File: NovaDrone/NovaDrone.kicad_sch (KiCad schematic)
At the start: 0 parts

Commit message: End of Inverter design
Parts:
- added C10, C11, C12, C13, C9: 15nF, Capacitor_SMD:C_0603_1608Metric, symbol Device:C
- added C3, C5, C7: 0.1uF, Capacitor_SMD:C_0603_1608Metric, symbol Device:C
- added D9: SS0540_R1_00001, BassingaLib_Diodes:SOD3816X135N, symbol BassingaLib_Diodes:SS0540_R1_00001
- added IC1, IC2, IC3: UCC27211DR, BassingaLib_BridgeDRVR:SOIC127P600X175-8N, symbol BassingaLib_BridgeDRVR:UCC27211DR
- added R17, R27, R29, R36, R37: 33k 1%, Resistor_SMD:R_0603_1608Metric, symbol Device:R
- added R26, R28, R30: 4.7k 1%, Resistor_SMD:R_0603_1608Metric, symbol Device:R
- added R31: 180k 1%, Resistor_SMD:R_0603_1608Metric, symbol Device:R
- added R32, R33, R34: 680R 1%, Resistor_SMD:R_0603_1608Metric, symbol Device:R
- added R35: 18k 1%, Resistor_SMD:R_0603_1608Metric, symbol Device:R
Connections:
- new net: C5.1, IC2.2 (HB)
- new net: C7.1, IC3.2 (HB)
- new net: C3.1, IC1.2 (HB)
- new net +10V: IC1.1 (VDD), IC2.1 (VDD), IC3.1 (VDD)
- new net +3.3V: D9.1 (K), R36.2
- new net GND: C12.1, C13.1, IC1.7 (VSS), IC2.7 (VSS), IC3.7 (VSS), R26.1, R28.1, R30.1, R35.1, R37.1
- new net Half-Bridge_1/G_H: IC1.3 (HO)
- new net Half-Bridge_1/G_L: IC1.8 (LO)
- new net Half-Bridge_1/HS: C3.2, IC1.4 (HS)
- new net Half-Bridge_1/Vshunt_B: R34.1
- new net Half-Bridge_2/G_H: IC2.3 (HO)
- new net Half-Bridge_2/G_L: IC2.8 (LO)
- new net Half-Bridge_2/HS: C5.2, IC2.4 (HS)
- new net Half-Bridge_2/Vshunt_B: R33.1
- new net Half-Bridge_3/G_H: IC3.3 (HO)
- new net Half-Bridge_3/G_L: IC3.8 (LO)
- new net Half-Bridge_3/HS: C7.2, IC3.4 (HS)
- new net Half-Bridge_3/Vshunt_B: R32.1
- new net OUT1: R17.1, R27.1, R29.1
- new net Phase_1: R17.2, R26.2, R27.2, R28.2, R29.2, R30.2
- new net Power_GND: C10.1, C11.1, C9.1
- new net V3.3_Mesure: C13.2, R36.1, R37.2
- new net Vbus_Mesure: C12.2, D9.2 (A), R31.1, R35.2
- new net Vshunt_1: C11.2, R34.2
- new net Vshunt_2: C10.2, R33.2
- new net Vshunt_3: C9.2, R32.2
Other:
- added sheet Half-Bridge_1 (Half_Bridge.kicad_sch)
- added sheet Half-Bridge_2 (Half_Bridge.kicad_sch)
- added sheet Half-Bridge_3 (Half_Bridge.kicad_sch)
- note added: "+3.3V Mesurement"
- note added: "Back-EMF Sensing"
- note added: "Half-Bridge Driver"
- note added: "PCB Temperature Mesurement"
- note added: "Power Invertor"
- note added: "Voltage Bus Mesurement"

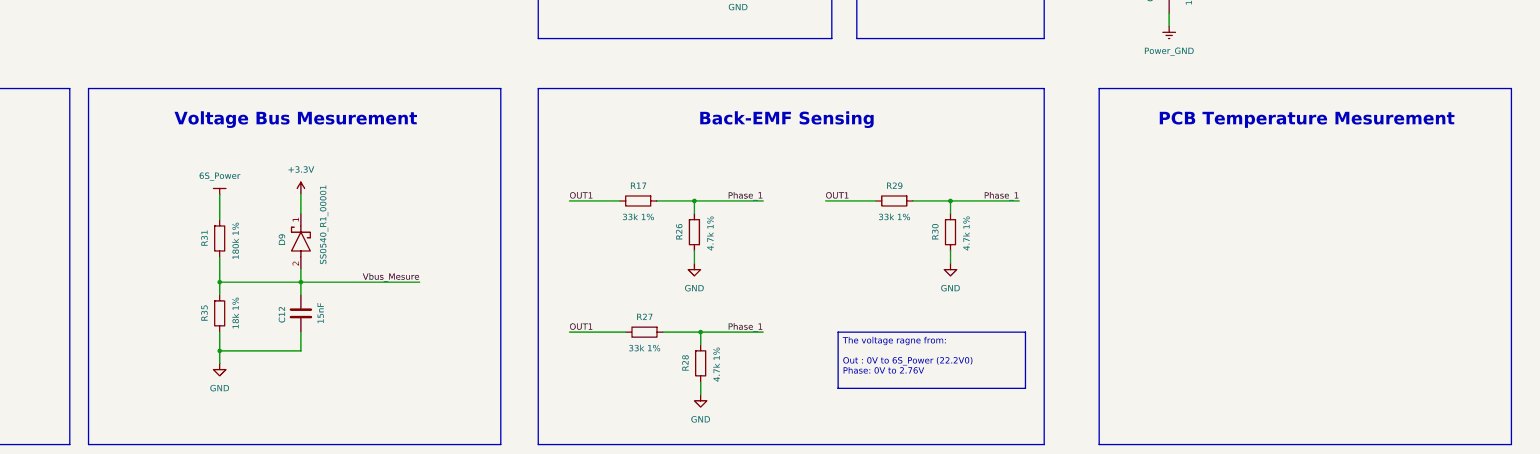
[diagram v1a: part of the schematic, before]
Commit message: PCB temperature measurement
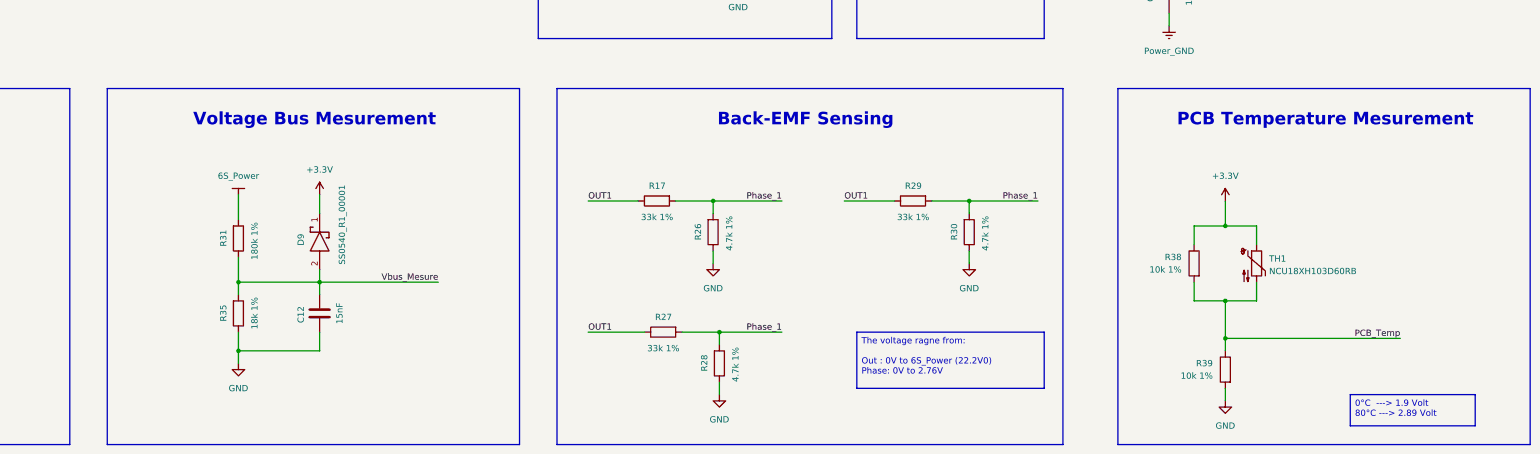
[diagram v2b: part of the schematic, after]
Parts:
- added R38, R39: 10k 1%, Resistor_SMD:R_0603_1608Metric, symbol Device:R
- added TH1: NCU18XH103D60RB, Resistor_SMD:R_0603_1608Metric, symbol Device:Thermistor_NTC
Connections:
- net +3.3V: now also R38.1, TH1.1
- net GND: now also R39.2
- new net PCB_Temp: R38.2, R39.1, TH1.2
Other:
- moved on the sheet: C12, D9, R17, R26, R27, R28, R29, R30, R31, R35

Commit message: Update 10.07.2025
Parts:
- added C14: 15nF, Capacitor_SMD:C_0603_1608Metric, symbol Device:C
- added D10: SS0540_R1_00001, BassingaLib_Diodes:SOD3816X135N, symbol BassingaLib_Diodes:SS0540_R1_00001
- added R40: 68k 1%, Resistor_SMD:R_0603_1608Metric, symbol Device:R
- added R42: 10k 1%, Resistor_SMD:R_0603_1608Metric, symbol Device:R
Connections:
- net +10V: now also R40.2
- net +3.3V: now also D10.1 (K)
- net GND: now also C14.1, R42.2
- net Phase_1: no longer R27.2, R28.2, R29.2, R30.2
- net MCU/PWM_C_H: now reaches IC3.5 (HI)
- net MCU/PWM_C_L: now reaches IC3.6 (LI)
- net MCU/PWM_A_H: now reaches IC1.5 (HI)
- net MCU/PWM_A_L: now reaches IC1.6 (LI)
- net MCU/PWM_B_H: now reaches IC2.5 (HI)
- net MCU/PWM_B_L: now reaches IC2.6 (LI)
- new net Phase_2: R29.2, R30.2
- new net Phase_3: R27.2, R28.2
- new net V10_Mesure: C14.2, D10.2 (A), R40.1, R42.1
- no-connect marks 0 -> 1
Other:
- added sheet MCU (MCU.kicad_sch)
- note added: "+10V Mesurement"
- moved on the sheet: C10, C11, C12, C13, C3, C5, C7, C9, D9, IC1, IC2, IC3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

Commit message: Interfaces Update
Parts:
- added C18, C19, C20, C34, C35: 1uF 50V, Capacitor_SMD:C_0805_2012Metric, symbol Device:C
- added C28, C29, C30: 0.1uF 50V, Capacitor_SMD:C_0603_1608Metric, symbol Device:C
- added D11: PESD2CANFD24V-TR, BassingaLib_TVS:SOT95P230X110-3N, symbol BassingaLib_TVS:PESD2CANFD24V-TR
- added D3: PESD3V3S2UT,215, BassingaLib_TVS:SOT95P230X110-3N, symbol BassingaLib_TVS:PESD3V3S2UT,215
- added IC5: TCAN3403DDFRQ1, BassinaLib_Com_Interfaces:SOT65P280X110-8N, symbol BassinaLib_Com_Interfaces:TCAN3403DDFRQ1
- added J1: JST SH 3Pin, BassinaLib_Connectors:JST_BM03B-SRSS-TB_LF__SN_, symbol BassinaLib_Connectors:BM03B-SRSS-TB_LF__SN_
- added J2: JST SH 5Pin, BassinaLib_Connectors:JST_BM05B-SRSS-TB_LF__SN_, symbol BassinaLib_Connectors:BM05B-SRSS-TB_LF__SN_
- added J3: JST SH 4Pin, BassinaLib_Connectors:ADAFRUIT_4328, symbol BassinaLib_Connectors:4328
- added R45, R46: 22R 1%, Resistor_SMD:R_0603_1608Metric, symbol Device:R
- added R47: 120R 1%, Resistor_SMD:R_0603_1608Metric, symbol Device:R
- added S1: DS04-254-2-01BK-SMT, BassinaLib_Switch:DS04254201BKSMT, symbol BassinaLib_Switch:DS04-254-2-01BK-SMT
- C3, C5, C7: value 0.1uF -> 0.1uF 50V
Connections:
- net +10V: now also C18.2, C19.2, C20.2
- net +3.3V: now also C34.1, C35.1, IC5.3 (V_CC), IC5.5 (VIO), J2.1, J3.1
- net GND: now also C18.1, C19.1, C20.1, C28.1, C29.1, C30.1, C34.2, C35.2, D11.3, D3.3, IC5.2 (GND), J1.2, J1.S1 (SHIELD), J1.S2 (SHIELD), J2.5, J2.S1 (SHIELD), J2.S2 (SHIELD), J3.4, J3.SH1 (SHIELD), J3.SH2 (SHIELD)
- net MCU/FDCAN2_RX: now also IC5.4 (RXD)
- net MCU/FDCAN2_TX: now also IC5.1 (TXD)
- net MCU/SWCLK: now also J2.3
- net MCU/SWDIO: now also J2.2
- net MCU/UART2_RX: now also D3.1, R46.2
- net MCU/UART2_TX: now also D3.2, R45.2
- net MCU/nRST: now also J2.4
- net Phase_1: now also C28.2
- net Phase_2: now also C30.2
- net Phase_3: now also C29.2
- new net: J1.1, R46.1
- new net: J1.3, R45.1
- new net: R47.2, S1.1
- new net CANH: D11.1, IC5.7 (CANH), J3.2, R47.1
- new net CANL: D11.2, IC5.6 (CANL), J3.3, S1.2
- new net MCU/FDCAN2_STB: IC5.8 (STB)
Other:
- sheet MCU ports: added FDCAN2_STB; removed none
- moved on the sheet: C10, C11, C12, C13, C14, C3, C5, C7, C9, D10, D9, IC1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

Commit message: Power Supply
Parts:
- removed J3: JST SH 4Pin, BassinaLib_Connectors:ADAFRUIT_4328, symbol BassinaLib_Connectors:4328
- added J3: JST PH 4Pin, BassinaLib_Connectors:S4B-PH-SM4-TB, symbol BassinaLib_Connectors:S4B-PH-SM4-TB_LF__SN_
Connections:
- net +3.3V: now also J3.1
- net CANH: now also J3.2
- net CANL: now also J3.3
- net GND: now also J3.4, J3.SH1 (SHIELD), J3.SH2 (SHIELD)
- net +10V renamed +12V
- net V10_Mesure renamed V12_Mesure
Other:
- added sheet Power_Supply (Power_Supply.kicad_sch)
- sheet MCU ports: added V12_Mesure; removed V10_Mesure
- note added: "+12V Mesurement"
- note removed: "+10V Mesurement"
